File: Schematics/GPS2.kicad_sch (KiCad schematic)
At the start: 1 part, among them J5 Conn_01x05_Pin

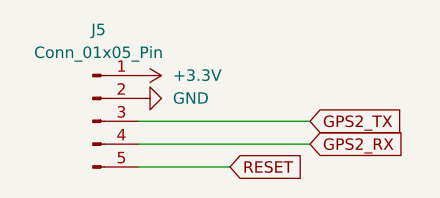
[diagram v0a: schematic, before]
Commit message: added LCSC numbers and footprint values, need to connect schemeatic pins, then can start layout
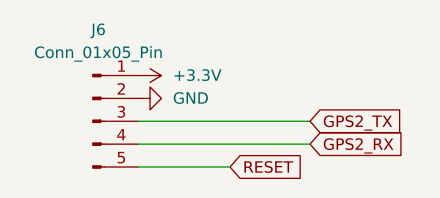
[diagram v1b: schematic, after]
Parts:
- J6: renamed from J5; LCSC Part (none) -> C157991
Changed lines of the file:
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@@
 		(dnp no)
 		(fields_autoplaced yes)
-		(property "Reference" "#PWR018"
+		(property "Reference" "#PWR056"
 			(at 123.19 69.85 0)
 			(effects
@@
 			(project "flightcomputer2"
 				(path "/6cb3dda3-5fe8-4715-b831-354360aa3199/9d9c275c-2a03-42ca-b9d6-2448b2e4b2af"
-					(reference "#PWR018")
+					(reference "#PWR056")
 					(unit 1)
 				)
@@
 		(dnp no)
 		(fields_autoplaced yes)
-		(property "Reference" "#PWR017"
+		(property "Reference" "#PWR055"
 			(at 113.03 67.31 0)
 			(effects
@@
 			(project "flightcomputer2"
 				(path "/6cb3dda3-5fe8-4715-b831-354360aa3199/9d9c275c-2a03-42ca-b9d6-2448b2e4b2af"
-					(reference "#PWR017")
+					(reference "#PWR055")
 					(unit 1)
 				)
@@
 		(dnp no)
 		(fields_autoplaced yes)
-		(property "Reference" "J5"
+		(property "Reference" "J6"
 			(at 112.395 62.23 0)
 			(effects
@@
 		)
 		(property "Description" "Generic connector, single row, 01x05, script generated"
+			(at 111.76 72.39 0)
+			(effects
+				(font
+					(size 1.27 1.27)
+				)
+				(hide yes)
+			)
+		)
+		(property "Sim.Device" ""
+			(at 111.76 72.39 0)
+			(effects
+				(font
+					(size 1.27 1.27)
+				)
+				(hide yes)
+			)
+		)
+		(property "Sim.Type" ""
+			(at 111.76 72.39 0)
+			(effects
+				(font
+					(size 1.27 1.27)
+				)
+				(hide yes)
+			)
+		)
+		(property "LCSC Part" "C157991"
 			(at 111.76 72.39 0)
 			(effects
@@
 			(project "flightcomputer2"
 				(path "/6cb3dda3-5fe8-4715-b831-354360aa3199/9d9c275c-2a03-42ca-b9d6-2448b2e4b2af"
-					(reference "J5")
+					(reference "J6")
 					(unit 1)
 				)
